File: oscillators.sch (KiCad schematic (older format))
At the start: 126 parts, among them U1 TL072-, U2 TL072-, U3 TL072-, U4 TA75S558F, U5 CD4052, U6 TL072-, U7 TL072-, U8 TL072-, U9 CD4052

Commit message: updated values, made some notes
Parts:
- R?: value 10K -> 100K
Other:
- note added: "Should there be a -10V reference here?"
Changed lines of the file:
@@
 P 11325 12025
 F 0 "R?" H 11225 12000 50  0000 C CNN
-F 1 "10K" H 11200 12075 50  0000 C CNN
+F 1 "100K" H 11200 12075 50  0000 C CNN
 F 2 "MyModules:SM0603-R-JRL" H 11325 12025 60  0001 C CNN
 F 3 "" H 11325 12025 60  0001 C CNN
@@
 	1    0    0    -1
 $EndComp
+Text Notes 3800 12375 0    60   ~ 0
+Should there be a -10V reference here?
 $EndSCHEMATC

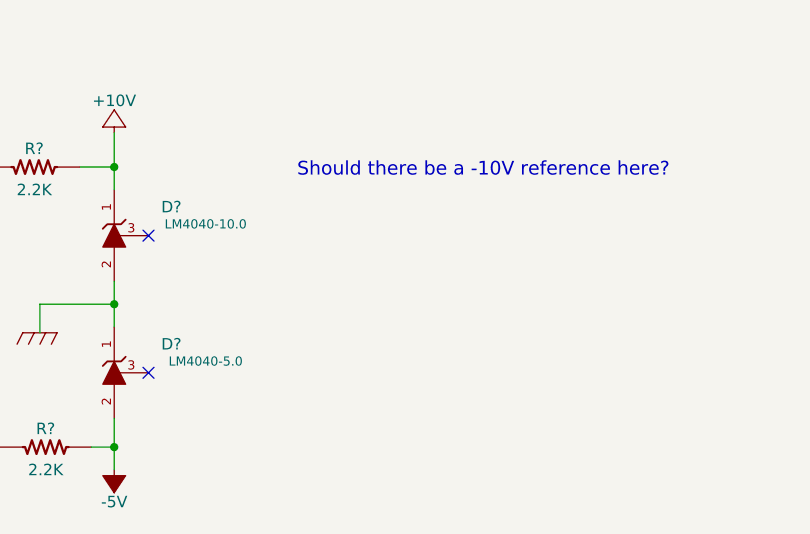
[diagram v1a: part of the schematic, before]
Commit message: added some notes about changes to +10V and -5V supplies
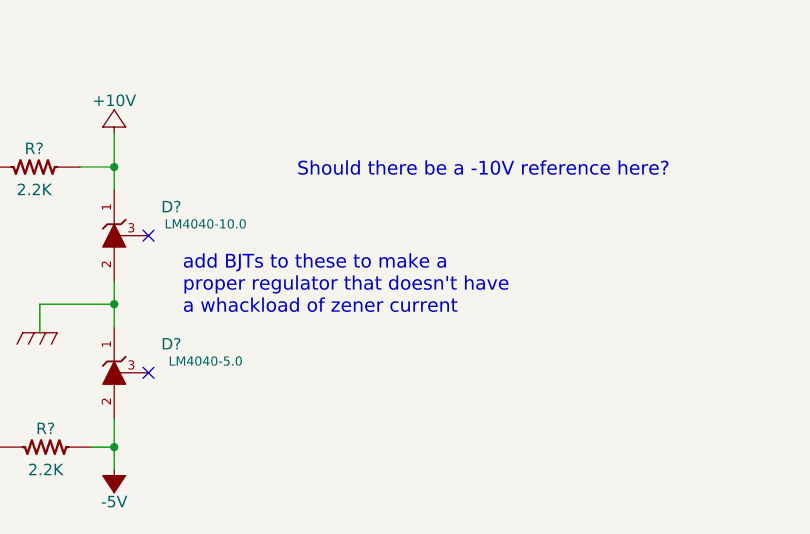
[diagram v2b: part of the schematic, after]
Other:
- note added: "add BJTs to these to make a\nproper regulator that doesn't have\na whackload of zener current"
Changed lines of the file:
@@
 Text Notes 3800 12375 0    60   ~ 0
 Should there be a -10V reference here?
+Text Notes 3300 12975 0    60   ~ 0
+add BJTs to these to make a\nproper regulator that doesn't have\na whackload of zener current
 $EndSCHEMATC

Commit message: added some notes about original Toshiba BJTs and FETs
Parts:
- added R? (x2): 100K, MyModules:SM0603-R-JRL, symbol R_US
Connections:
- net VCO1_XMOD: now also R?.2
- net at C?.2, R?.1, R?.2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: now also R?.2
- new net VCO1_MOD_SUM: R?.1
- new net VCO2_MOD_SUM: R?.1
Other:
- note added: "TOSHIBA NPN\nmatched pair?"
- note removed: "add BJTs to these to make a\nproper regulator that doesn't have\na whackload of zener current"
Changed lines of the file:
@@
 	1    0    0    -1
 $EndComp
-Text GLabel 15525 8550 0    60   Input ~ 0
+Text GLabel 15575 8550 0    60   Input ~ 0
 KCV_2
 $Comp
@@
 	0    -1   -1   0
 $EndComp
-Text GLabel 15725 9125 0    60   Input ~ 0
+Text GLabel 15625 9125 0    60   Input ~ 0
 VCO2_MOD
 Text GLabel 1500 9425 0    60   Input ~ 0
@@
 	2275 9425 1500 9425
 Wire Wire Line
-	15725 9125 15750 9125
+	15625 9125 15750 9125
 Connection ~ 16300 9125
 Wire Wire Line
@@
 	16300 8350 16300 9725
 Wire Wire Line
-	15525 8550 15725 8550
+	15575 8550 15725 8550
 Connection ~ 17000 8550
 Wire Notes Line
@@
 Text Notes 3800 12375 0    60   ~ 0
 Should there be a -10V reference here?
-Text Notes 3300 12975 0    60   ~ 0
-add BJTs to these to make a\nproper regulator that doesn't have\na whackload of zener current
+Text GLabel 1425 8875 0    60   Input ~ 0
+VCO1_MOD_SUM
+Text GLabel 15600 8850 0    60   Input ~ 0
+VCO2_MOD_SUM
+$Comp
+L R_US R?
+U 1 1 58657F6C
+P 1900 8875
+F 0 "R?" V 1980 8875 50  0000 C CNN
+F 1 "100K" V 1800 8875 50  0000 C CNN
+F 2 "MyModules:SM0603-R-JRL" H 1900 8875 60  0001 C CNN
+F 3 "" H 1900 8875 60  0001 C CNN
+F 4 "P91.0KCCT-ND" V 1900 8875 60  0001 C CNN "Digikey"
+	1    1900 8875
+	0    -1   -1   0
+$EndComp
+Wire Wire Line
+	2100 8875 2275 8875
+Connection ~ 2275 8875
+Wire Wire Line
+	1700 8875 1425 8875
+$Comp
+L R_US R?
+U 1 1 58659749
+P 15950 8850
+F 0 "R?" V 16030 8850 50  0000 C CNN
+F 1 "100K" V 15850 8850 50  0000 C CNN
+F 2 "MyModules:SM0603-R-JRL" H 15950 8850 60  0001 C CNN
+F 3 "" H 15950 8850 60  0001 C CNN
+F 4 "P91.0KCCT-ND" V 15950 8850 60  0001 C CNN "Digikey"
+	1    15950 8850
+	0    -1   -1   0
+$EndComp
+Wire Wire Line
+	16150 8850 16300 8850
+Connection ~ 16300 8850
+Wire Wire Line
+	15750 8850 15600 8850
+Text Notes 6975 7725 0    60   ~ 0
+TOSHIBA NPN\nmatched pair?
+Text Notes 21150 8000 0    60   ~ 0
+TOSHIBA NPN\nmatched pair?
 $EndSCHEMATC

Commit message: changing transistor matched pairs
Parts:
- removed Q?: PMP4201G, TO_SOT_Packages_SMD:SOT-353, symbol PMP4201G
- added Q? (x3): PMP4201G, TO_SOT_Packages_SMD:SOT-353, symbol PMP4201G
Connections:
- net GND: now also Q?.3 (B), Q?.3 (B)
- net at Q?.1 (B): now also R?.2, TC?.1
- net at Q?.2 (E): now also R?.2, Q?.2 (E)
- net at R?.1, U2.2 (-): now also Q?.4 (C); no longer Q?.5 (C)
- net at R?.1, U7.2 (-): now also Q?.4 (C)
- net at C?.1, R?.1, U1.6 (-): now also Q?.5 (C)
- net at R?.2, TC?.1: now also Q?.1 (B)
- net at C?.1, R?.1, U6.6 (-): now also Q?.5 (C)
- net at R?.2: now also Q?.2 (E), Q?.2 (E)
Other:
- moved on the sheet: Q?A
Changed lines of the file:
@@
 Connection ~ 20900 7800
 Wire Wire Line
-	21000 8525 21000 8650
+	21000 8450 21000 8650
 Wire Wire Line
 	20325 9200 20000 9200
@@
 Connection ~ 6825 7800
 Wire Wire Line
-	6925 8525 6925 8650
+	6925 8450 6925 8650
 Wire Wire Line
 	6250 9200 5925 9200
@@
 L PMP4201G Q?
 U 1 1 5813321B
-P 6925 8250
-F 0 "Q?" H 6900 8325 50  0000 L CNN
-F 1 "PMP4201G" H 7125 8400 50  0000 L CNN
-F 2 "TO_SOT_Packages_SMD:SOT-353" H 6350 7925 50  0001 L CIN
-F 3 "" H 6725 8250 50  0000 L CNN
-	1    6925 8250
-	1    0    0    -1
-$EndComp
-$Comp
-L PMP4201G Q?
-U 1 1 581366EE
-P 21000 8250
-F 0 "Q?" H 20975 8325 50  0000 L CNN
-F 1 "PMP4201G" H 21200 8400 50  0000 L CNN
-F 2 "TO_SOT_Packages_SMD:SOT-353" H 20425 7925 50  0001 L CIN
-F 3 "" H 20800 8250 50  0000 L CNN
-	1    21000 8250
+P 6725 8250
+F 0 "Q?" H 6575 8425 50  0000 L CNN
+F 1 "PMP4201G" H 6300 8100 50  0000 L CNN
+F 2 "TO_SOT_Packages_SMD:SOT-353" H 6150 7925 50  0001 L CIN
+F 3 "" H 6525 8250 50  0000 L CNN
+	1    6725 8250
 	1    0    0    -1
 $EndComp
@@
 Text Notes 21150 8000 0    60   ~ 0
 TOSHIBA NPN\nmatched pair?
+$Comp
+L PMP4201G Q?
+U 2 1 591A1DBF
+P 7125 8250
+F 0 "Q?" H 6975 8425 50  0000 L CNN
+F 1 "PMP4201G" H 6675 8000 50  0001 L CNN
+F 2 "TO_SOT_Packages_SMD:SOT-353" H 6550 7925 50  0001 L CIN
+F 3 "" H 6925 8250 50  0000 L CNN
+	2    7125 8250
+	-1   0    0    -1
+$EndComp
+Wire Wire Line
+	6825 8450 7025 8450
+Connection ~ 6925 8450
+$Comp
+L PMP4201G Q?
+U 1 1 591A8357
+P 20800 8250
+F 0 "Q?" H 20650 8425 50  0000 L CNN
+F 1 "PMP4201G" H 20375 8100 50  0000 L CNN
+F 2 "TO_SOT_Packages_SMD:SOT-353" H 20225 7925 50  0001 L CIN
+F 3 "" H 20600 8250 50  0000 L CNN
+	1    20800 8250
+	1    0    0    -1
+$EndComp
+$Comp
+L PMP4201G Q?
+U 2 1 591A835D
+P 21200 8250
+F 0 "Q?" H 21050 8425 50  0000 L CNN
+F 1 "PMP4201G" H 20750 8000 50  0001 L CNN
+F 2 "TO_SOT_Packages_SMD:SOT-353" H 20625 7925 50  0001 L CIN
+F 3 "" H 21000 8250 50  0000 L CNN
+	2    21200 8250
+	-1   0    0    -1
+$EndComp
+Wire Wire Line
+	20900 8450 21100 8450
+Connection ~ 21000 8450
 $EndSCHEMATC

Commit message: litte bit of work again - added tri sym CVs
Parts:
- removed D?: LM4040-10.0, symbol LM4040
- removed D?: LM4040-5.0, symbol LM4040
- removed R? (x2): 2.2K, MyModules:SM0603-R-JRL, symbol R_US
- added D? (x2): LM4040-10.0, MyModules:SOT23-132-JRL, symbol LM4040
- added D?: LM4040-5.0, MyModules:SOT23-132-JRL, symbol LM4040
- added R? (x3): 2.2K, MyModules:SM0603-R-JRL, symbol R_US
- added R? (x2): 47K, MyModules:SM0603-R-JRL, symbol R_US
- added R? (x2): 22K, MyModules:SM0603-R-JRL, symbol R_US
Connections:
- net +10V: now also D?.1 (K), R?.2
- net +12V: now also R?.1
- net -12V: now also R?.1, R?.1; no longer R?.1, R?.1
- net -5V: now also U5.8 (VSS), D?.2 (A), R?.2
- net GND: now also D?.1 (K), D?.1 (K), D?.2 (A); no longer U5.8 (VSS)
- net at C?.2, D?.1 (K), Q?.1 (D)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: now also R?.1; no longer Q?.1 (B)
- net at C?.2, D?.1 (K), Q?.1 (D)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: now also R?.1; no longer Q?.1 (B)
- new net: Q?.1 (B), R?.1, R?.2 (x2)
- new net -10V: D?.2 (A), R?.1, R?.1, R?.2
- new net VCO1_TRI_SYM: R?.2
- new net VCO2_TRI_SYM: R?.2
- no-connect marks 12 -> 13
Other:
- note added: "Need to add TRI SYMMETRY CV here"
- note removed: "'Ultrafast' switching BJT"
- note removed: "No reference voltage \nhere. -10V on JP8. May \nneed to adjust R."
- note removed: "PMBT2369 seems like\nvery close substitute, even \nslightly faster"
- note removed: "Should there be a -10V reference here?"
- moved on the sheet: D?, Q?, R?

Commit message: added DDR3 240 connector, starting to connect input and output labels
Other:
- note added: "GND CMOS INPUTS?"
- note removed: "Need to add TRI SYMMETRY CV here"
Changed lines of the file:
@@
 	-1   0    0    1
 $EndComp
-Text Notes 8025 9650 0    60   ~ 0
-Need to add TRI SYMMETRY CV here
 $Comp
 L R_US R?
@@
 Connection ~ 23075 9975
 Connection ~ 23075 10275
+Text Notes 14750 13025 1    60   ~ 0
+GND CMOS INPUTS?
+Text Notes 28675 13025 1    60   ~ 0
+GND CMOS INPUTS?
 $EndSCHEMATC

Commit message: more connector connecting. about to annotate
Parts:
- removed Q? (x4): PMP4201G, TO_SOT_Packages_SMD:SOT-353, symbol PMP4201G
- added Q? (x4): 2SC4207, MyModules:SOT753_TSOP5_SC-74A, symbol 2SC4207
- Q?: footprint SOT-23 -> MyModules:SOT416-SC75
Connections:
- net GND: now also Q?.3 (B), Q?.3 (B)
- net at R?.2, TC?.1: now also Q?.1 (B) (x2)
- net at R?.2: now also Q?.2 (E), Q?.2 (E) (x2)
- net at C?.1, R?.1, U1.6 (-): now also Q?.5 (C)
- net at R?.1, U2.2 (-): now also Q?.4 (C)
- net at C?.1, R?.1, U6.6 (-): now also Q?.5 (C)
- net at R?.1, U7.2 (-): now also Q?.4 (C)
- net VCO1_TUNE renamed VCO1_INIT
- net VCO2_TUNE renamed VCO2_INIT
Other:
- note removed: "TOSHIBA NPN\nmatched pair?"
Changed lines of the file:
@@
 $EndComp
 Text GLabel 2000 7100 0    60   Input ~ 0
-VCO1_TUNE
+VCO1_INIT
 Text Notes 1450 7000 0    60   ~ 0
 set initial pitch
@@
 $EndComp
 Text GLabel 16025 7100 0    60   Input ~ 0
-VCO2_TUNE
+VCO2_INIT
 Text Notes 15475 7000 0    60   ~ 0
 set initial pitch
@@
 	1    0    0    -1
 $EndComp
-$Comp
-L PMP4201G Q?
-U 1 1 5813321B
-P 6725 8250
-F 0 "Q?" H 6575 8425 50  0000 L CNN
-F 1 "PMP4201G" H 6300 8100 50  0000 L CNN
-F 2 "TO_SOT_Packages_SMD:SOT-353" H 6150 7925 50  0001 L CIN
-F 3 "" H 6525 8250 50  0000 L CNN
-	1    6725 8250
-	1    0    0    -1
-$EndComp
 Text Notes 12575 12850 0    60   ~ 0
 NPN here is 2SC752-Y
@@
 F 0 "Q?" H 24050 9050 50  0000 L CNN
 F 1 "2SA1832" H 24050 9125 50  0000 L CNN
-F 2 "SOT-23" H 24075 8975 50  0001 L CIN
+F 2 "MyModules:SOT416-SC75" H 24075 8975 50  0001 L CIN
 F 3 "" H 23875 9050 50  0000 L CNN
 	1    23875 9050
@@
 	1    15950 8850
 	0    -1   -1   0
-$EndComp
-Text Notes 6975 7725 0    60   ~ 0
-TOSHIBA NPN\nmatched pair?
-Text Notes 21150 8000 0    60   ~ 0
-TOSHIBA NPN\nmatched pair?
-$Comp
-L PMP4201G Q?
-U 2 1 591A1DBF
-P 7125 8250
-F 0 "Q?" H 6975 8425 50  0000 L CNN
-F 1 "PMP4201G" H 6675 8000 50  0001 L CNN
-F 2 "TO_SOT_Packages_SMD:SOT-353" H 6550 7925 50  0001 L CIN
-F 3 "" H 6925 8250 50  0000 L CNN
-	2    7125 8250
-	-1   0    0    -1
-$EndComp
-$Comp
-L PMP4201G Q?
-U 1 1 591A8357
-P 20800 8250
-F 0 "Q?" H 20650 8425 50  0000 L CNN
-F 1 "PMP4201G" H 20375 8100 50  0000 L CNN
-F 2 "TO_SOT_Packages_SMD:SOT-353" H 20225 7925 50  0001 L CIN
-F 3 "" H 20600 8250 50  0000 L CNN
-	1    20800 8250
-	1    0    0    -1
-$EndComp
-$Comp
-L PMP4201G Q?
-U 2 1 591A835D
-P 21200 8250
-F 0 "Q?" H 21050 8425 50  0000 L CNN
-F 1 "PMP4201G" H 20750 8000 50  0001 L CNN
-F 2 "TO_SOT_Packages_SMD:SOT-353" H 20625 7925 50  0001 L CIN
-F 3 "" H 21000 8250 50  0000 L CNN
-	2    21200 8250
-	-1   0    0    -1
 $EndComp
 $Comp
@@
 Text Notes 28675 13025 1    60   ~ 0
 GND CMOS INPUTS?
+$Comp
+L 2SC4207 Q?
+U 1 1 5A924FB5
+P 6725 8250
+F 0 "Q?" H 6450 8525 50  0000 L CNN
+F 1 "2SC4207" H 6450 8450 50  0000 L CNN
+F 2 "MyModules:SOT753_TSOP5_SC-74A" H 6925 8175 50  0001 L CIN
+F 3 "" H 6725 8250 50  0000 L CNN
+	1    6725 8250
+	1    0    0    -1
+$EndComp
+$Comp
+L 2SC4207 Q?
+U 2 1 5A924FBC
+P 7125 8250
+F 0 "Q?" H 7000 8525 50  0000 L CNN
+F 1 "2SC4207" H 6825 8450 50  0000 L CNN
+F 2 "MyModules:SOT753_TSOP5_SC-74A" H 7325 8175 50  0001 L CIN
+F 3 "" H 7125 8250 50  0000 L CNN
+	2    7125 8250
+	-1   0    0    -1
+$EndComp
+$Comp
+L 2SC4207 Q?
+U 1 1 5A9273C3
+P 20800 8250
+F 0 "Q?" H 20525 8525 50  0000 L CNN
+F 1 "2SC4207" H 20525 8450 50  0000 L CNN
+F 2 "MyModules:SOT753_TSOP5_SC-74A" H 21000 8175 50  0001 L CIN
+F 3 "" H 20800 8250 50  0000 L CNN
+	1    20800 8250
+	1    0    0    -1
+$EndComp
+$Comp
+L 2SC4207 Q?
+U 2 1 5A9289DD
+P 21200 8250
+F 0 "Q?" H 20925 8525 50  0000 L CNN
+F 1 "2SC4207" H 20925 8450 50  0000 L CNN
+F 2 "MyModules:SOT753_TSOP5_SC-74A" H 21400 8175 50  0001 L CIN
+F 3 "" H 21200 8250 50  0000 L CNN
+	2    21200 8250
+	-1   0    0    -1
+$EndComp
 $EndSCHEMATC
